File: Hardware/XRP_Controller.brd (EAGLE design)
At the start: 63.5 x 54 mm, 208 parts, among them J1 POWER_JACKPOWER_JACK_SLOT, J12 Vertical Qwiic Connector, J13 Vertical Qwiic Connector, J14 Vertical Qwiic Connector, J3 JST_6_PIN_VERTICAL, J4 JST_6_PIN_VERTICAL, J5 JST_6_PIN_VERTICAL, J6 JST_6_PIN_VERTICAL, J9 Vertical Qwiic Connector, Q3 20V/4.2A/52mΩ/1.4W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

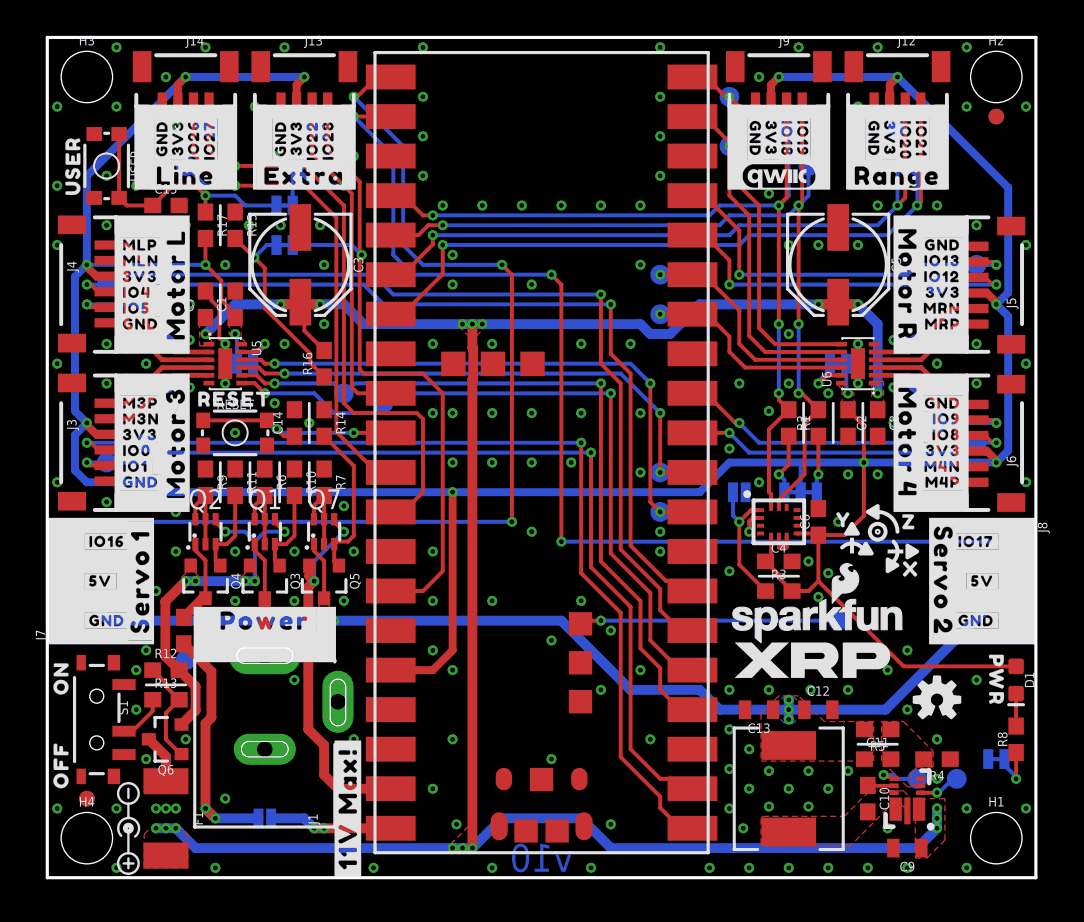
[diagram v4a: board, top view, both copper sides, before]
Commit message: Minor routing improvments
Nudge a couple traces to improve GND continuity
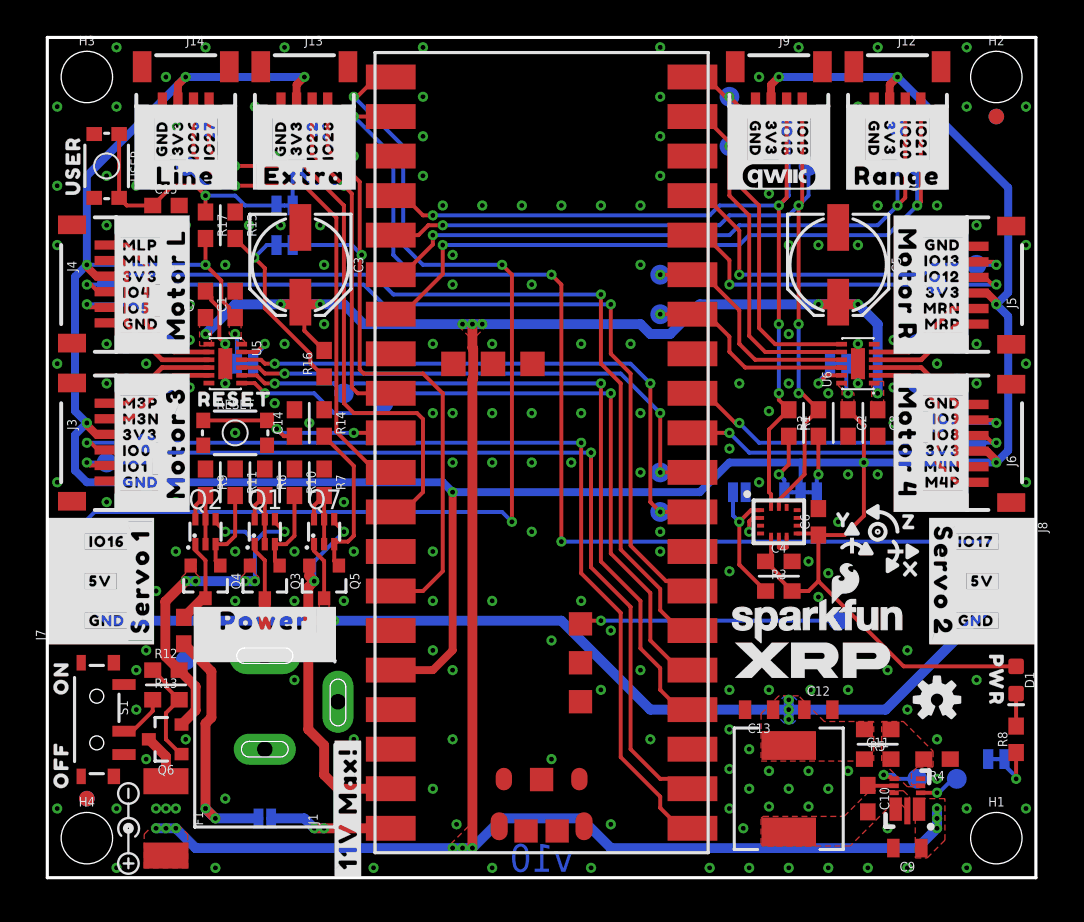
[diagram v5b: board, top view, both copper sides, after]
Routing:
- net RP_IO16/S1_OUT: track 66.6 -> 67.1 mm
- net GND: vias 196 -> 197
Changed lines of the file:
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@@
 <via x="19.685" y="20.955" extent="1-16" drill="0.3048"/>
 <via x="8.255" y="20.955" extent="1-16" drill="0.3048"/>
-<via x="8.255" y="23.495" extent="1-16" drill="0.3048"/>
+<via x="8.255" y="24.13" extent="1-16" drill="0.3048"/>
 <via x="12.065" y="28.575" extent="1-16" drill="0.3048"/>
-<via x="19.05" y="23.876" extent="1-16" drill="0.3048"/>
+<via x="19.05" y="24.13" extent="1-16" drill="0.3048"/>
 <via x="39.37" y="20.955" extent="1-16" drill="0.3048"/>
 <via x="5.715" y="13.335" extent="1-16" drill="0.3048"/>
@@
 <via x="26.035" y="40.005" extent="1-16" drill="0.3048"/>
 <via x="24.765" y="17.78" extent="1-16" drill="0.3048"/>
+<via x="58.42" y="24.13" extent="1-16" drill="0.3048"/>
 </signal>
 <signal name="3.3V">
@@
 <wire x1="1.778" y1="26.162" x2="2.54" y2="25.4" width="0.508" layer="16"/>
 <wire x1="1.778" y1="28.448" x2="1.778" y2="26.162" width="0.508" layer="16"/>
-<wire x1="6.985" y1="24.765" x2="26.035" y2="24.765" width="0.508" layer="16"/>
 <wire x1="52.451" y1="26.67" x2="48.387" y2="26.67" width="0.508" layer="16"/>
 <wire x1="48.387" y1="26.67" x2="43.815" y2="26.67" width="0.508" layer="16"/>
@@
 <wire x1="10.16" y1="41.06" x2="10.16" y2="39.37" width="0.254" layer="1"/>
 <wire x1="2.54" y1="25.4" x2="6.35" y2="25.4" width="0.508" layer="16"/>
-<wire x1="6.35" y1="25.4" x2="6.985" y2="24.765" width="0.508" layer="16"/>
+<wire x1="6.35" y1="25.4" x2="25.4" y2="25.4" width="0.508" layer="16"/>
+<wire x1="26.035" y1="24.765" x2="25.4" y2="25.4" width="0.508" layer="16"/>
 <wire x1="8.39" y1="49.67" x2="8.39" y2="50.935" width="0.508" layer="1"/>
 <wire x1="8.39" y1="50.935" x2="8.89" y2="51.435" width="0.508" layer="1"/>
@@
 <contactref element="U1" pad="21"/>
 <via x="29.845" y="22.86" extent="1-16" drill="0.3048"/>
-<wire x1="2.413" y1="22.86" x2="1.143" y2="21.59" width="0.254" layer="16"/>
-<wire x1="29.845" y1="22.86" x2="2.413" y2="22.86" width="0.254" layer="16"/>
+<wire x1="3.048" y1="23.495" x2="1.143" y2="21.59" width="0.254" layer="16"/>
+<wire x1="29.845" y1="22.86" x2="29.21" y2="23.495" width="0.254" layer="16"/>
+<wire x1="29.21" y1="23.495" x2="3.048" y2="23.495" width="0.254" layer="16"/>
 <via x="29.21" y="39.37" extent="1-16" drill="0.3048"/>
 <wire x1="29.21" y1="39.37" x2="29.845" y2="38.735" width="0.254" layer="1"/>
@@
 <wire x1="60.96" y1="39.37" x2="60.77" y2="39.56" width="0.254" layer="1"/>
 <wire x1="60.77" y1="39.56" x2="59.69" y2="39.56" width="0.254" layer="1"/>
-<wire x1="44.45" y1="38.735" x2="55.245" y2="38.735" width="0.254" layer="16"/>
+<wire x1="44.45" y1="38.735" x2="56.261" y2="38.735" width="0.254" layer="16"/>
 <contactref element="U1" pad="17"/>
 <wire x1="41.44" y1="43.815" x2="42.202" y2="43.815" width="0.254" layer="1"/>
@@
 <wire x1="44.45" y1="41.567" x2="42.202" y2="43.815" width="0.254" layer="1"/>
 <contactref element="TP14" pad="1"/>
-<wire x1="55.245" y1="38.735" x2="55.88" y2="39.37" width="0.254" layer="16"/>
-<wire x1="55.88" y1="39.37" x2="59.69" y2="39.37" width="0.254" layer="16"/>
+<wire x1="56.261" y1="38.735" x2="56.896" y2="39.37" width="0.254" layer="16"/>
+<wire x1="56.896" y1="39.37" x2="59.69" y2="39.37" width="0.254" layer="16"/>
 <wire x1="59.69" y1="39.37" x2="60.96" y2="39.37" width="0.254" layer="16"/>
 </signal>
@@
 <wire x1="17.78" y1="16.51" x2="18.415" y2="16.51" width="0.635" layer="16"/>
 <wire x1="18.415" y1="16.51" x2="33.02" y2="16.51" width="0.635" layer="16"/>
-<wire x1="33.02" y1="16.51" x2="37.465" y2="12.065" width="0.635" layer="16"/>
-<wire x1="37.465" y1="12.065" x2="41.91" y2="12.065" width="0.635" layer="16"/>
 <via x="47.625" y="10.16" extent="1-16" drill="0.3048"/>
 <via x="47.625" y="11.43" extent="1-16" drill="0.3048"/>
@@
 <vertex x="46.736" y="10.541"/>
 </polygon>
-<wire x1="41.91" y1="12.065" x2="43.18" y2="10.795" width="0.635" layer="16"/>
-<wire x1="43.18" y1="10.795" x2="47.625" y2="10.795" width="0.635" layer="16"/>
+<wire x1="33.02" y1="16.51" x2="38.735" y2="10.795" width="0.635" layer="16"/>
+<wire x1="38.735" y1="10.795" x2="47.625" y2="10.795" width="0.635" layer="16"/>
 <wire x1="47.625" y1="10.16" x2="47.625" y2="10.795" width="0.635" layer="16"/>
 <wire x1="47.625" y1="11.43" x2="47.625" y2="10.795" width="0.635" layer="16"/>

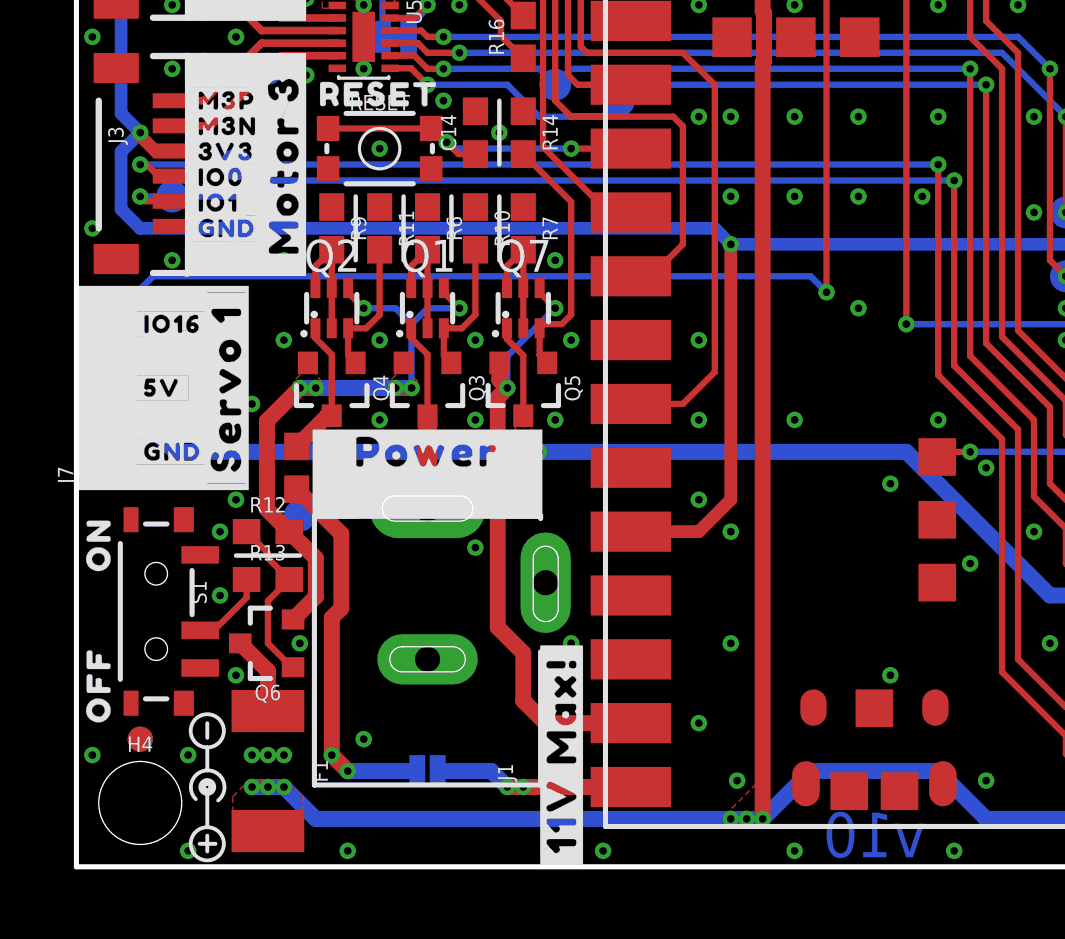
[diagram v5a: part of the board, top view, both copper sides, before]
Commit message: Update VUSB path
Replace R18 with 2x 1206 10 Ohm resistors in parallel (better power rating than a single 0603)
Change VUSB jumper from NO to NC
Flip 3V3 and VBUS pins of Pico W footprint
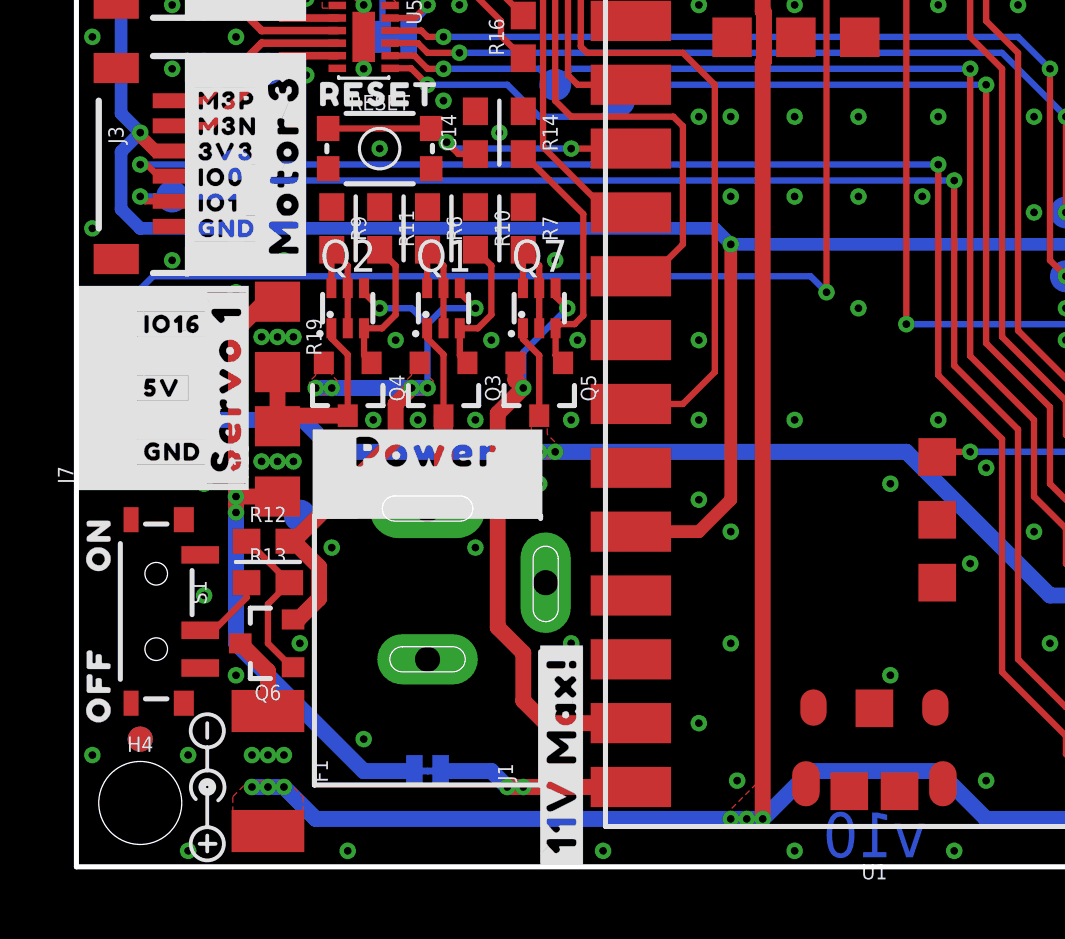
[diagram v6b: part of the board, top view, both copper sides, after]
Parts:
- added R19: 10, SparkFun-Resistors:1206
- R18: value 4.7 -> 10; device SparkFun-Resistors:0603 -> SparkFun-Resistors:1206
- VUSB: value JUMPER-SMT_2_NO_SILK -> JUMPER-SMT_2_NC_TRACE_SILK; device SparkFun-Jumpers:SMT-JUMPER_2_NO_SILK -> SparkFun-Jumpers:SMT-JUMPER_2_NC_TRACE_SILK
- moved R18 0.80 mm to (8.00, 16.1), turned to 90 degrees
- moved Q1 0.63 mm to (14.6, 22.2)
- moved Q2 0.63 mm to (10.8, 22.2)
- moved Q3 0.63 mm to (14.6, 19.1)
- moved Q4 0.63 mm to (10.8, 19.1)
- moved Q5 0.63 mm to (18.4, 19.1)
- moved Q7 0.63 mm to (18.4, 22.2)
- moved R12 0.38 mm to (7.62, 13.0)
- moved R13 0.13 mm to (7.62, 11.3)
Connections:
- net N$18: now also R18.1, R19.1; no longer R18.2
- net V_USB: now also R18.2, R19.2; no longer R18.1
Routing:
- net N$18: track 16.0 -> 26.1 mm
- net V_USB: track 5.65 -> 8.87 mm
- net V_POW: track 24.4 -> 25.7 mm
- net GND: vias 197 -> 201

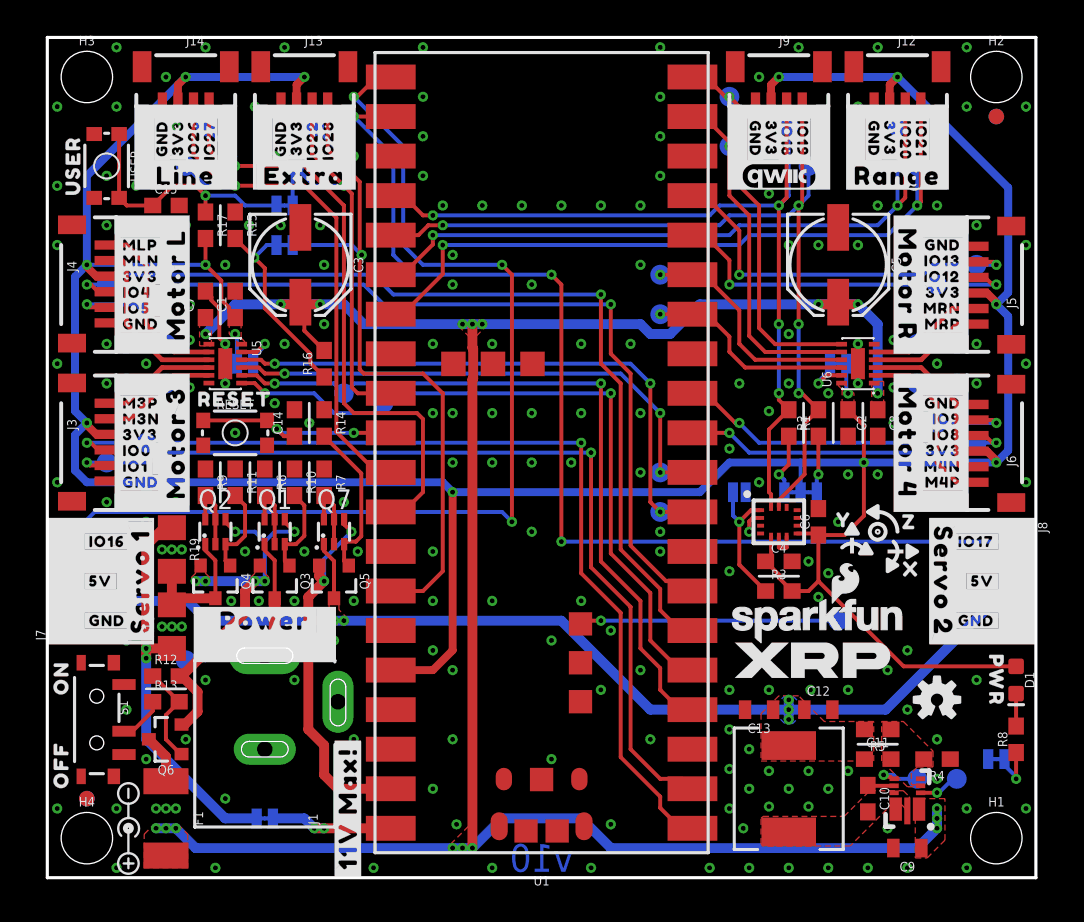
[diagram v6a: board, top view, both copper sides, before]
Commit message: Design review updates
Add IO22 silk label to user button
Move VUSB jumper under V_SYS label in schematic
Renumber last few test points
Add test point for IMU interrupt pin
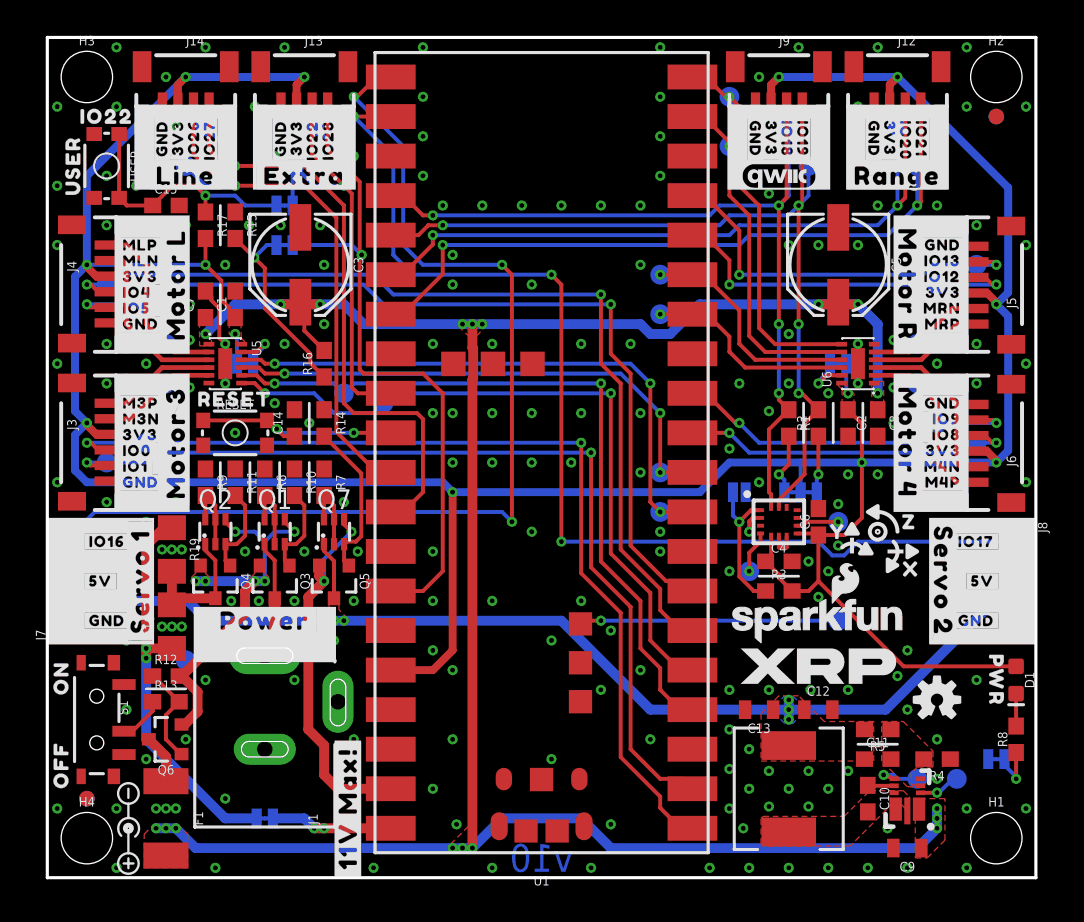
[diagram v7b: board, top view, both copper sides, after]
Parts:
- added TP38, TP39: TEST-POINT3X5, SparkFun-Connectors:PAD.03X.05
- added U$68: (no value), output:IO220
- moved TP34 50.1 mm to (8.89, 14.0)
- moved TP37 42.0 mm to (50.8, 16.5)
- moved TP36 11.4 mm to (55.9, 6.35)
- moved U$81 2.54 mm to (54.0, 23.5)
- moved TP35 2.54 mm to (58.4, 6.35)
- moved U$79 2.44 mm to (51.2, 19.6)
- moved U$80 1.17 mm to (56.1, 21.7)
- moved U$89 0.85 mm to (50.8, 22.2)
- moved U$65 0.54 mm to (49.5, 13.6)
- turned VUSB to 180 degrees
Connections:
- new net IMU_INT1: TP38.1, U4.4
- new net IMU_INT2: TP39.1, U4.9
- net 5V_EN: now also TP35.1; no longer TP34.1
- net 5V_PG: now also TP36.1; no longer TP35.1
- net BOOTSEL: now also TP37.1; no longer TP36.1
- net N$18: now also VUSB.1; no longer VUSB.2
- net N$9: now also VUSB.2; no longer VUSB.1
- net V_BATT: now also TP34.1; no longer TP37.1
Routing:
- net IMU_INT2: track 0.00 -> 2.74 mm, vias 0 -> 1
- net IMU_INT1: track 0.00 -> 2.73 mm, vias 0 -> 1
- net RP_IO17/S2_OUT: track 69.7 -> 70.5 mm
- net GND: vias 201 -> 202
